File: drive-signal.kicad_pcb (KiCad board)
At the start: 2 copper layers, 43.2 x 67.8 mm, 30 parts, among them J1 Conn_01x03_Pin, J10 Conn_01x04_Pin, J11 Conn_01x04_Pin, J2 Conn_01x03_Pin, J3 Conn_01x03_Pin, J4 Conn_01x03_Pin, J5 JETSON, J6 IMU, J7 Conn_01x02_Pin, J8 Conn_01x04_Pin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

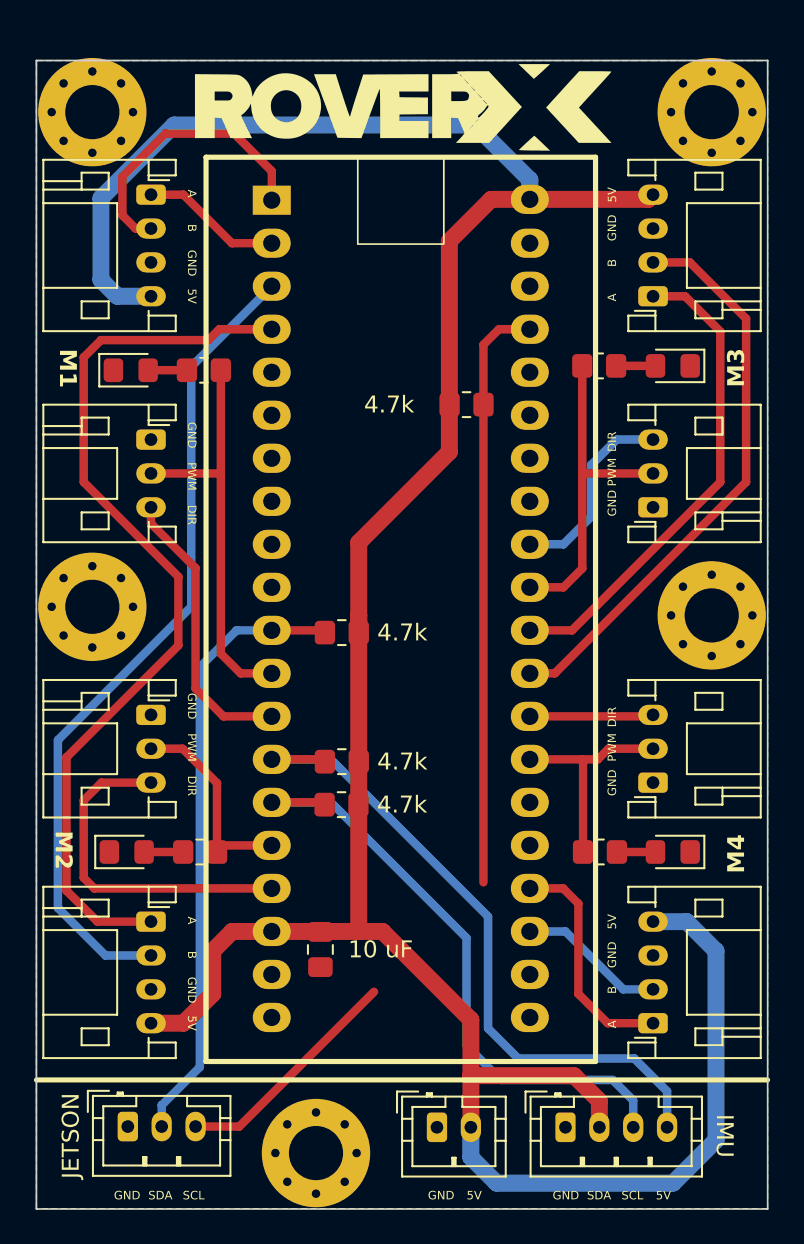
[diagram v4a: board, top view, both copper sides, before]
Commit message: change physical dims to use via-ed holes
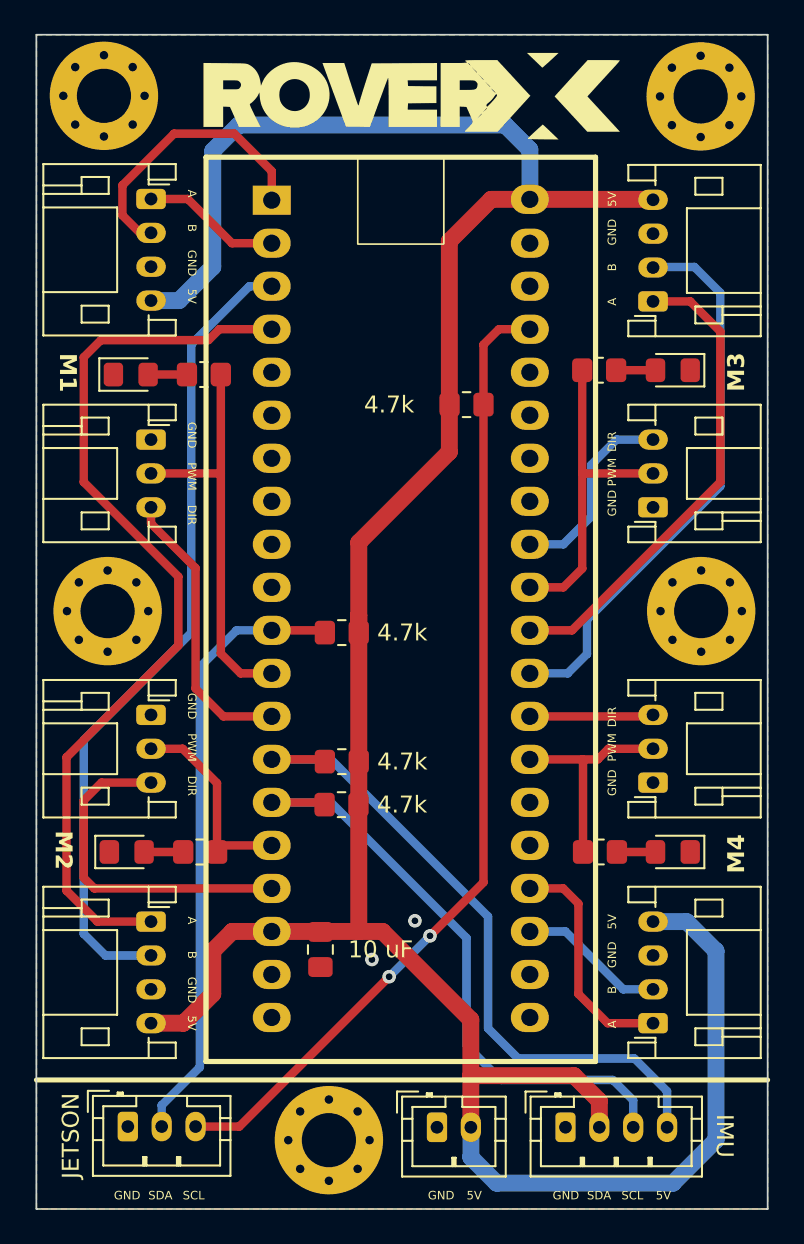
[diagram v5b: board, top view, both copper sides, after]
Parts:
- moved H2 1.18 mm to (50.7, 30.5)
- moved H1 1.14 mm to (86.0, 30.6)
- moved H5 1.08 mm to (64.0, 92.2)
- moved H3 0.94 mm to (50.9, 61.0)
- moved H4 0.67 mm to (86.0, 61.0)
- moved J11 0.30 mm to (83.1, 42.7)
- moved D2 0.25 mm to (52.3, 47.0)
- moved J8 0.25 mm to (53.5, 36.6)
- moved R6 0.25 mm to (56.6, 47.0)
- moved D4 0.25 mm to (84.3, 46.7)
- moved R8 0.25 mm to (80.0, 46.7)
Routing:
- net I2C2_J_SCL: track 48.7 -> 57.8 mm, vias 0 -> 2
- net +5V: track 169.4 -> 165.4 mm
- net RB_B: track 34.0 -> 33.2 mm
- net GND: vias 0 -> 2
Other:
- board size 43.2 x 67.8 mm -> 43.2 x 69.3 mm
